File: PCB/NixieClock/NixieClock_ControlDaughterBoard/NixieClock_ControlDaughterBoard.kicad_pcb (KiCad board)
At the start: 2 copper layers, 85 x 50 mm, 30 parts, among them J1 Conn_01x05, J3 Conn_01x04_Pin, J4 Conn_01x04_Pin, Q1 IRLML6244, Q2 IRLML6244

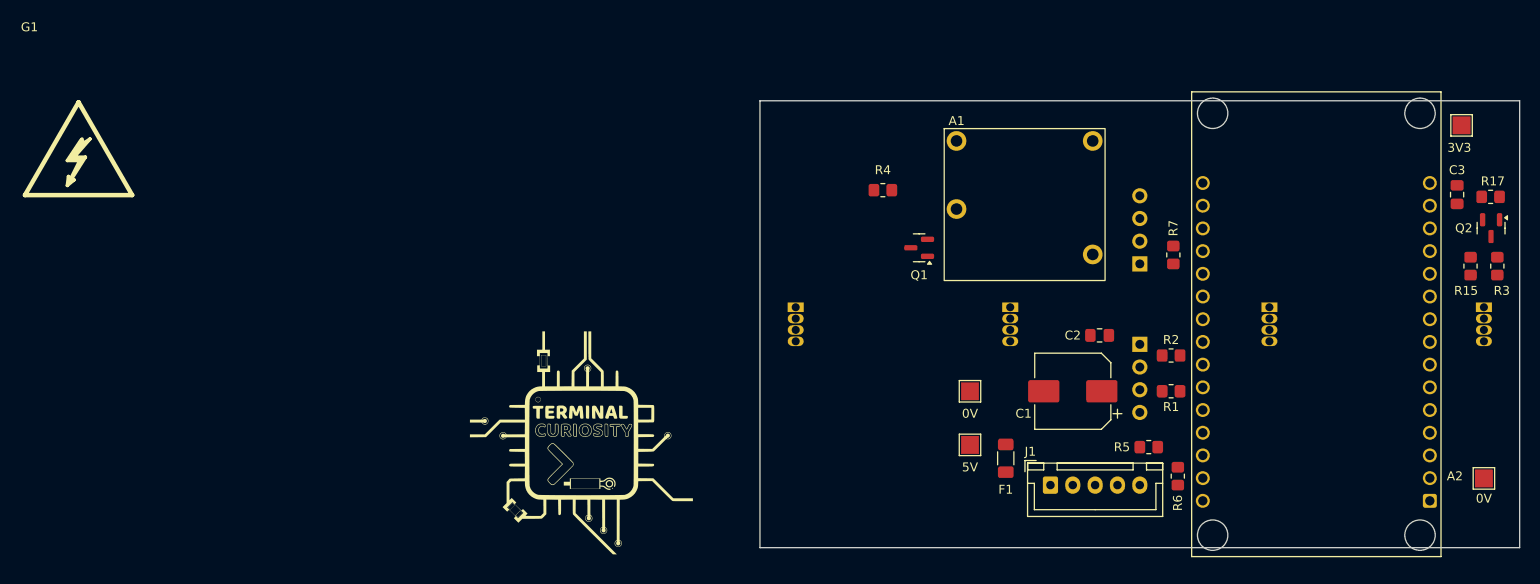
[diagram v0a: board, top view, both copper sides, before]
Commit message: Layout WIP
layout half completed.
+5V net class added to SCH so it has thicker traces on PCB
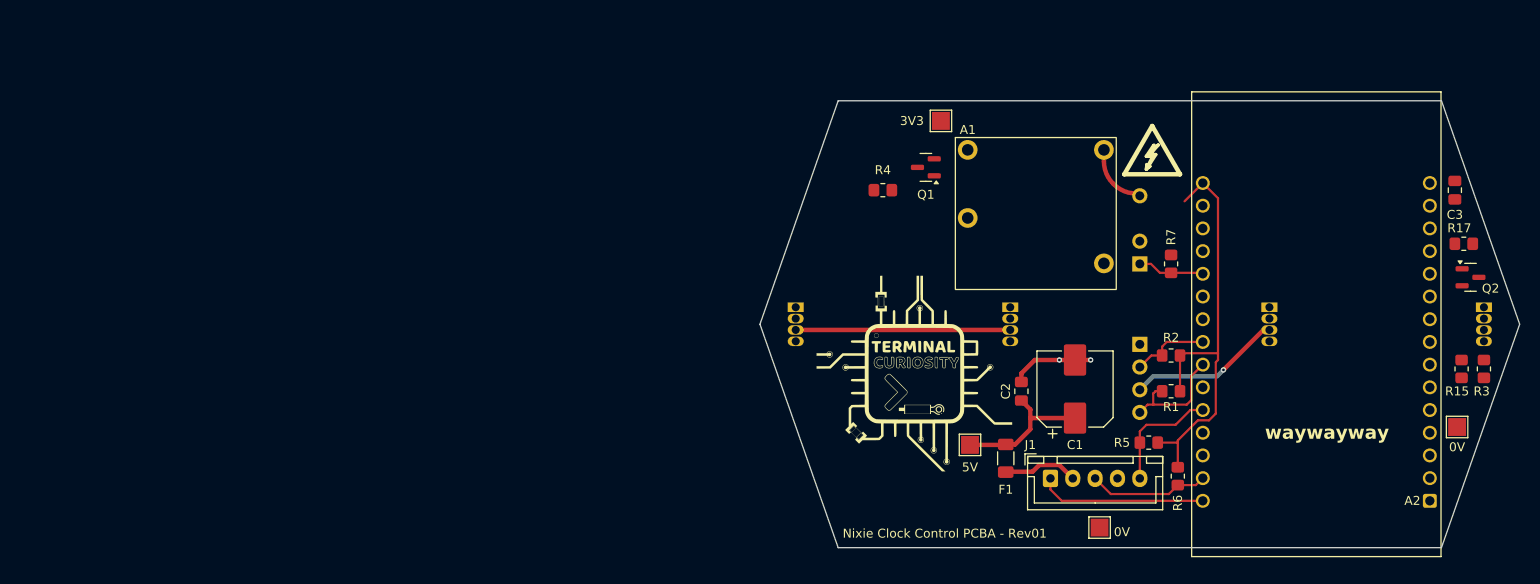
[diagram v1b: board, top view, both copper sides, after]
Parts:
- moved G1 120.2 mm to (144.0, 92.2)
- moved TP2 58.3 mm to (126.2, 82.2)
- moved G2 38.0 mm to (123.2, 110.5)
- moved TP5 21.0 mm to (144.0, 127.8)
- moved R3 11.6 mm to (187.0, 110.0), turned to 90 degrees
- moved R15 11.5 mm to (184.5, 110.0), turned to -90 degrees
- moved C2 10.8 mm to (135.2, 112.5), turned to 90 degrees
- moved Q1 9.03 mm to (124.6, 87.5)
- moved TP6 6.49 mm to (184.0, 116.5)
- moved R17 6.05 mm to (184.8, 96.0), turned to 0 degrees
- moved Q2 5.96 mm to (185.5, 99.8), turned to 0 degrees
- moved A1 1.60 mm to (127.9, 84.1)
- moved R7 1.03 mm to (152.0, 98.2)
- moved J1 0.75 mm to (138.5, 122.2)
- moved C3 0.56 mm to (183.8, 90.0)
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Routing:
- net +5V: track 0.00 -> 57.4 mm, vias 0 -> 1
- net +3.3V: track 0.00 -> 48.9 mm
- net /INT2: track 0.00 -> 18.8 mm
- net /I2C_SCL2: track 0.00 -> 13.5 mm
- net /I2C_SDA2: track 0.00 -> 13.3 mm
- net /I2C_SCL1: track 0.00 -> 13.2 mm
- net GND: track 0.00 -> 9.33 mm, vias 0 -> 2
- net /I2C_SDA1: track 0.00 -> 8.80 mm
- net /5V_IN: track 0.00 -> 8.43 mm
- net /LDR_IN: track 0.00 -> 7.51 mm
- net Net-(A1-VOUT): track 0.00 -> 6.19 mm
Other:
- outline, holes or cut-outs redrawn
- board text added: "Nixie Clock Control PCBA - Rev01"
- board text added: "waywayway"

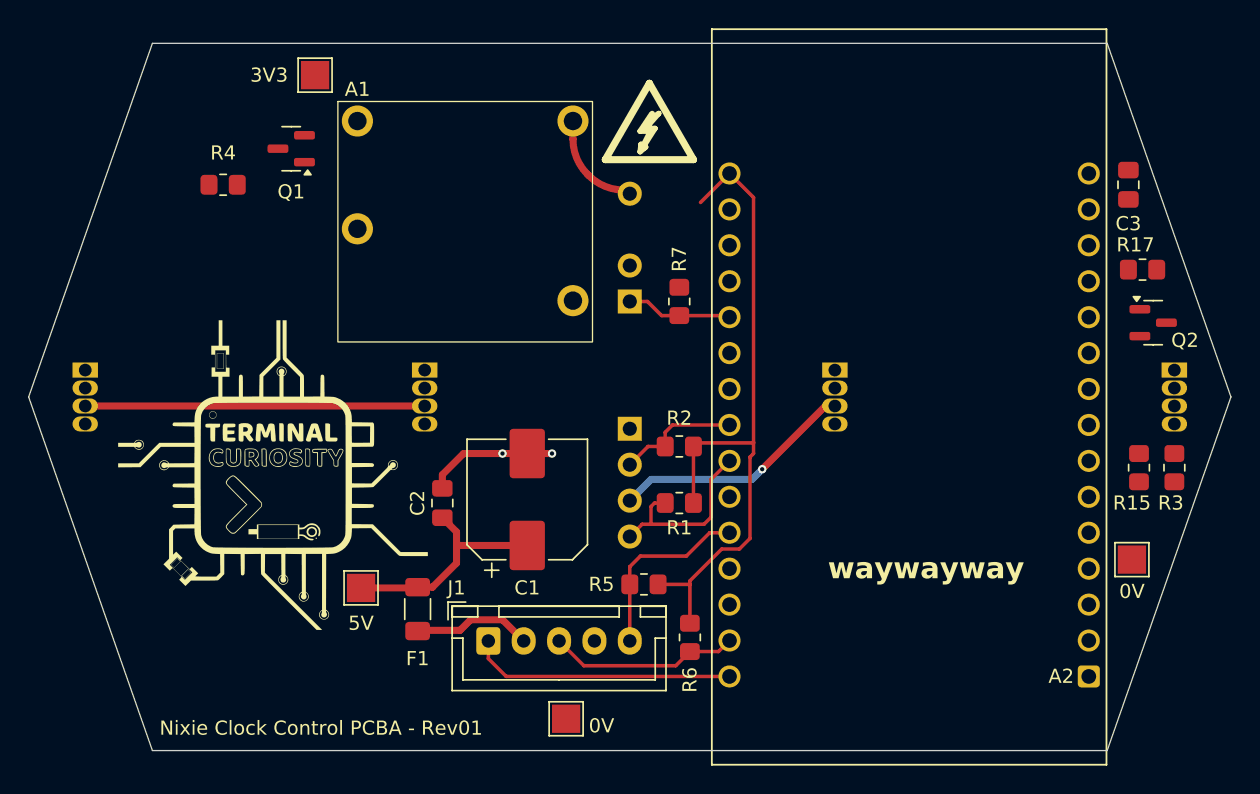
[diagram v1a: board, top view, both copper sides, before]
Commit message: layout draft1 complete
completed all pcb routing and polygon pour.
Changed LED footprints to wide pins. previously they had 0.085mm clearance between pads, which is too tight to manufacture. wide pins have 0.36mm min (14mil) which is above PCBway suggested 6mil.
Removed all DRC errors.
Some warnings exist for ESP32 silkscreen beyond board border, but this is ok for the assembly overall
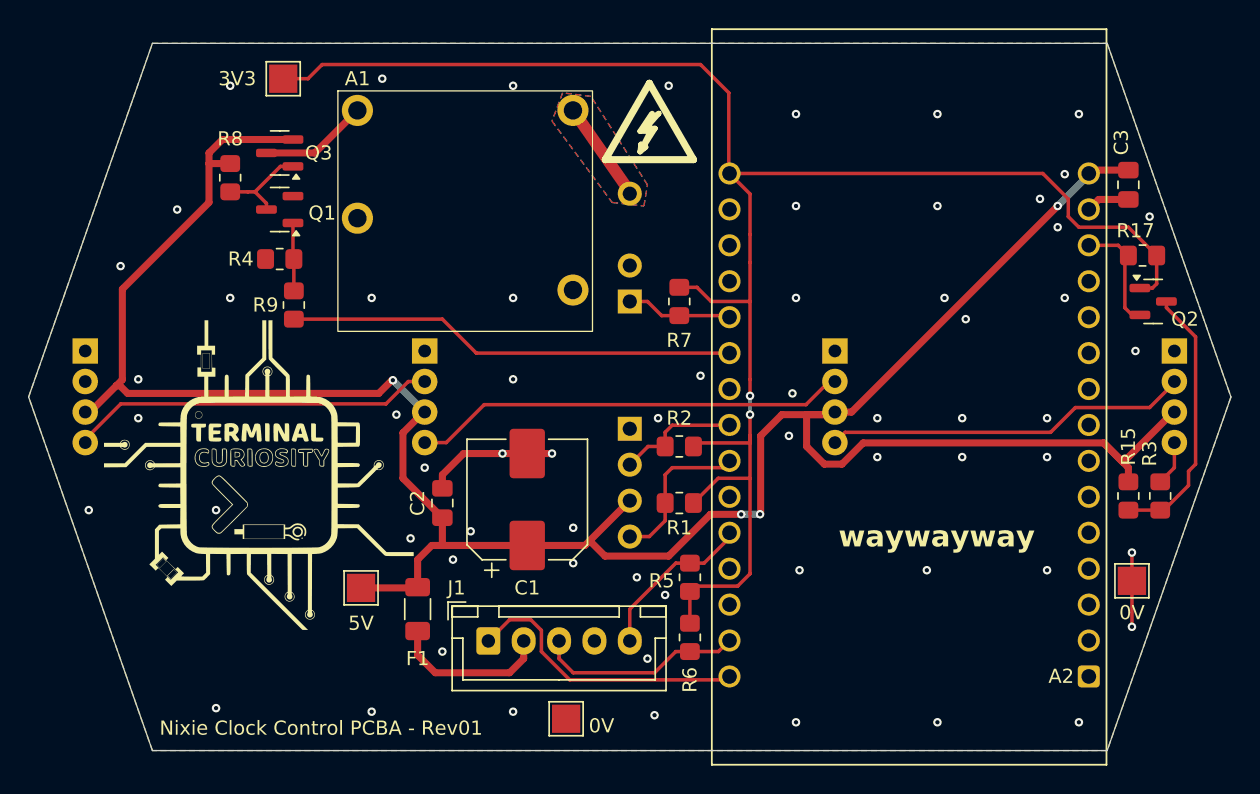
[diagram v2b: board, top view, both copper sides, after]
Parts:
- added Q3: IRLML6402, Package_TO_SOT_SMD:SOT-23, F.Cu at (123.8, 87.8)
- added R8: 10k, Resistor_SMD:R_0805_2012Metric_Pad1.20x1.40mm_HandSolder, F.Cu at (120.2, 89.5)
- added R9: 470R, Resistor_SMD:R_0805_2012Metric_Pad1.20x1.40mm_HandSolder, F.Cu at (124.8, 98.5)
- D1, D2, D3, D4: footprint LED_THT:LED_D5.0mm-4_RGB -> LED_THT:LED_D5.0mm-4_RGB_Wide_Pins
- moved R4 6.60 mm to (123.8, 95.2), turned to 180 degrees
- moved Q1 4.38 mm to (123.8, 91.8)
- moved R5 3.29 mm to (152.8, 117.8), turned to 90 degrees
- moved TP2 2.26 mm to (124.0, 82.5)
- moved R3 2.24 mm to (186.0, 112.0)
- moved R15 2.14 mm to (183.8, 112.0)
- moved Q2 1.50 mm to (185.5, 98.2)
- moved TP6 1.50 mm to (184.0, 118.0)
- moved D1 1.35 mm to (187.0, 101.8)
- moved D2 1.35 mm to (163.0, 101.8)
- moved D3 1.35 mm to (134.0, 101.8)
- moved D4 1.35 mm to (110.0, 101.8)
- moved G2 1.00 mm to (122.2, 110.5)
- moved R17 1.00 mm to (184.8, 95.0), turned to 180 degrees
- moved A1 0.75 mm to (127.9, 83.4)
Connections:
- A1 pad 1: +5V -> Net-(A1-VIN)
- A1 pad 2: Net-(Q1-D) -> GND
- Q1 pad 1: Net-(A2-GPIO16/RX2) -> Net-(Q1-G)
- R4 pad 1: Net-(A2-GPIO16/RX2) -> Net-(Q1-G)
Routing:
- net +5V: track 57.4 -> 177.8 mm, vias 1 -> 4
- net +3.3V: track 48.9 -> 125.8 mm, vias 0 -> 2
- net Net-(A2-GPIO16/RX2): track 0.00 -> 32.1 mm
- net Net-(D2-DOUT): track 0.77 -> 31.0 mm
- net Net-(D3-DOUT): track 0.00 -> 26.1 mm
- net Net-(D1-DOUT): track 0.00 -> 25.6 mm
- net /LED-Data_5V: track 0.00 -> 19.0 mm
- net GND: track 9.33 -> 17.7 mm, vias 2 -> 63
- net /LED-Data_3V3: track 0.00 -> 8.17 mm
- net Net-(A1-VIN): track 0.00 -> 7.68 mm
- net Net-(Q1-D): track 0.00 -> 6.77 mm
- net Net-(Q1-G): track 0.00 -> 4.83 mm
- net Net-(D1-DIN): track 0.00 -> 3.19 mm
- net /5V_IN: track 8.43 -> 11.4 mm
- net /I2C_SCL1: track 13.2 -> 11.2 mm
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- added copper zone on B.Cu, net GND
- added copper zone on F.Cu, net GND
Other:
- board text added: "OK to add teardrops"

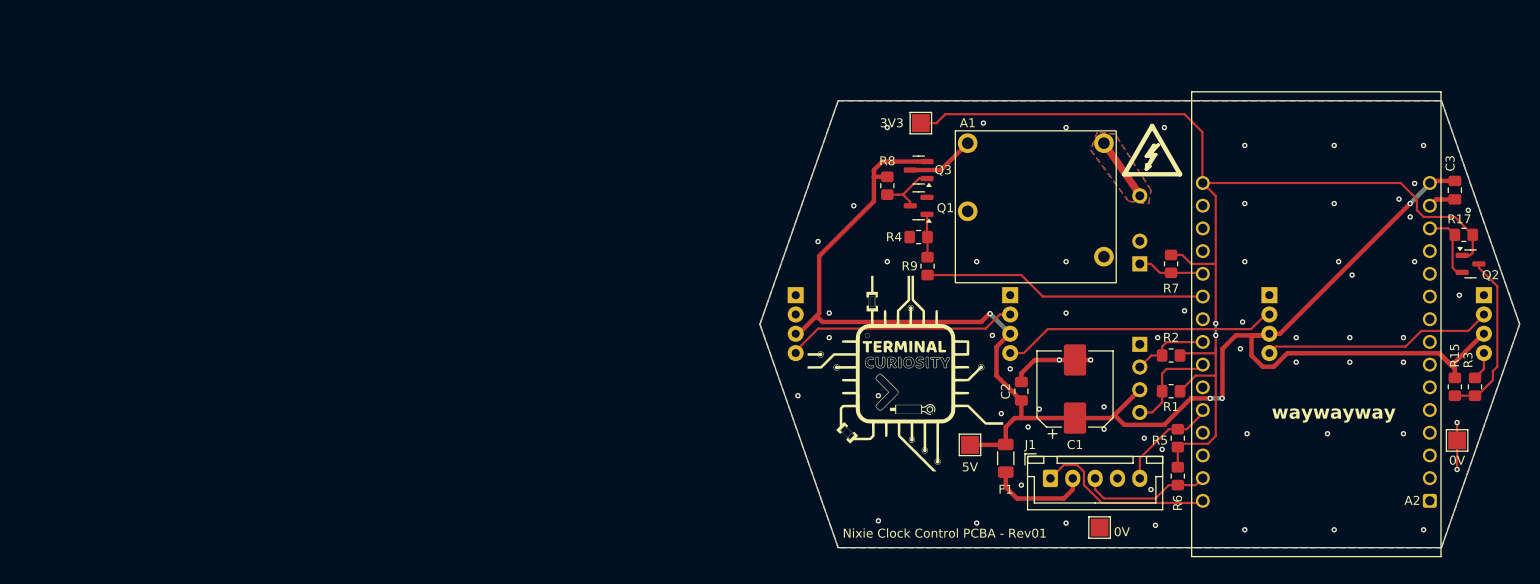
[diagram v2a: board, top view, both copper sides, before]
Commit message: PCB layout 2 complete
layout 1 was incorrect as the connectors and LEDs were not located in the right place to correctly mate with the tube panel PCBA. When connectors and LEDs were moved, all the traces became scrambled. it was necessary to re-wire the entire board.
ESP32 pins were also remapped to improve ease of wiring
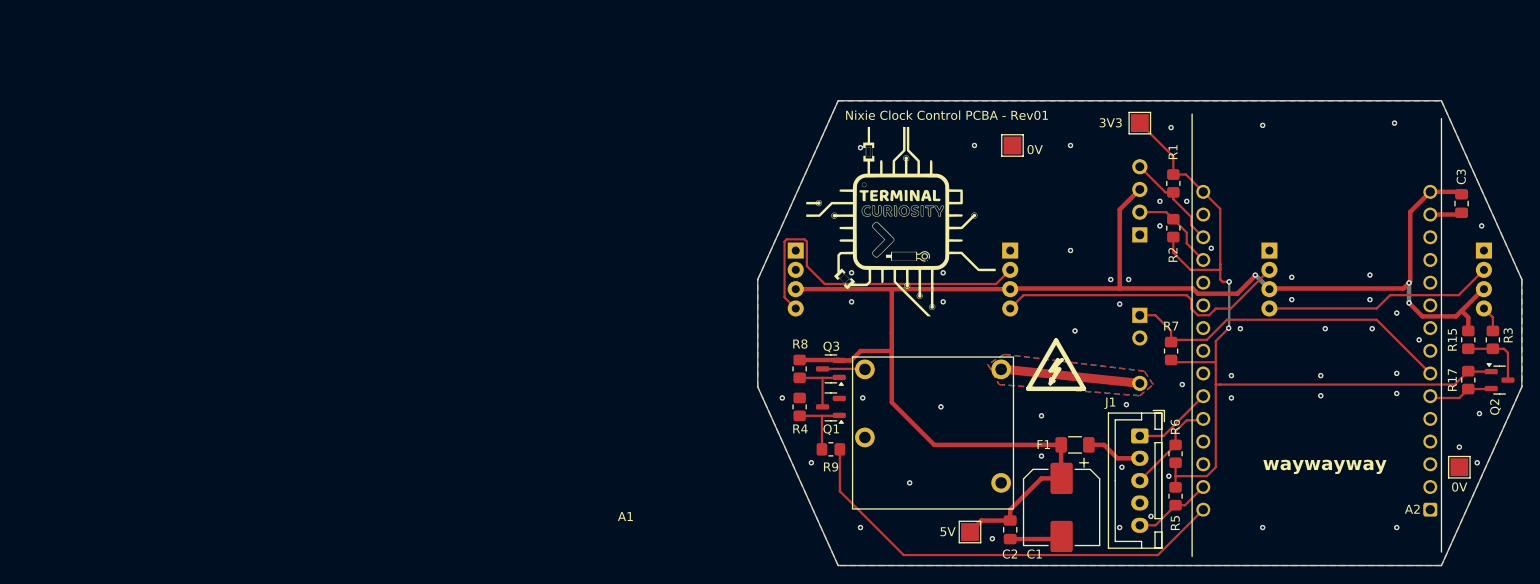
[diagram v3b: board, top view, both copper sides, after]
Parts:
- moved TP5 43.8 mm to (134.2, 85.0)
- moved A1 27.8 mm to (116.4, 108.7)
- moved G1 26.3 mm to (133.2, 116.2)
- moved Q1 24.5 mm to (113.9, 114.2)
- moved TP2 24.5 mm to (148.5, 82.5)
- moved Q3 24.3 mm to (113.9, 110.0)
- moved R1 23.3 mm to (152.2, 89.2), turned to -90 degrees
- moved R4 23.2 mm to (110.4, 114.2), turned to 90 degrees
- moved R9 23.2 mm to (113.9, 119.0), turned to 180 degrees
- moved R8 22.7 mm to (110.4, 110.0)
- moved G2 17.0 mm to (121.8, 93.5)
- moved R17 16.3 mm to (185.2, 111.2), turned to -90 degrees
- moved C2 15.6 mm to (134.0, 128.0), turned to -90 degrees
- moved R2 14.3 mm to (152.2, 94.2), turned to 90 degrees
- moved Q2 13.4 mm to (188.8, 111.2)
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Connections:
- A2 pad 13: /LED-Data_3V3 -> unconnected-(A2-GPIO13-Pad13)
- A2 pad 18: unconnected-(A2-GPIO15-Pad18) -> /I2C_SCL1
- A2 pad 19: unconnected-(A2-GPIO2-Pad19) -> /I2C_SDA1
- A2 pad 20: /LDR_IN -> unconnected-(A2-GPIO4-Pad20)
- A2 pad 21: Net-(A2-GPIO16/RX2) -> unconnected-(A2-GPIO16/RX2-Pad21)
- A2 pad 23: /I2C_SDA1 -> unconnected-(A2-GPIO5-Pad23)
- A2 pad 24: /I2C_SCL1 -> unconnected-(A2-GPIO18-Pad24)
- A2 pad 25: unconnected-(A2-GPIO19-Pad25) -> /INT2
- A2 pad 30: /INT2 -> Net-(A2-GPIO23)
- A2 pad 6: unconnected-(A2-GPIO32-Pad6) -> /LED-Data_3V3
- A2 pad 7: unconnected-(A2-GPIO33-Pad7) -> /LDR_IN
- J1 pad 3: /I2C_SCL2 -> /I2C_SDA2
- J1 pad 5: /I2C_SDA2 -> /I2C_SCL2
- R5 pad 2: /I2C_SDA2 -> /I2C_SCL2
- R6 pad 2: /I2C_SCL2 -> /I2C_SDA2
- R9 pad 1: Net-(A2-GPIO16/RX2) -> Net-(A2-GPIO23)
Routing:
- net Net-(A2-GPIO23): track 0.00 -> 50.4 mm
- net Net-(A2-GPIO16/RX2): track 32.1 -> 0.00 mm
- net /LDR_IN: track 7.51 -> 37.6 mm
- net +3.3V: track 125.8 -> 97.1 mm
- net Net-(D3-DOUT): track 26.1 -> 37.7 mm
- net /INT2: track 20.4 -> 8.94 mm
- net /LED-Data_5V: track 19.0 -> 7.68 mm
- net Net-(A1-VOUT): track 7.05 -> 15.7 mm
- net GND: track 17.7 -> 9.45 mm, vias 63 -> 55
- net /I2C_SCL2: track 14.7 -> 8.88 mm
- net /5V_IN: track 11.4 -> 6.32 mm
- net +5V: track 177.8 -> 174.3 mm, vias 4 -> 3
- net Net-(Q1-G): track 4.83 -> 7.91 mm
- net Net-(A1-VIN): track 7.68 -> 4.76 mm
- net Net-(D2-DOUT): track 31.0 -> 33.2 mm
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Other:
- board size 85 x 50 mm -> 85.5 x 52 mm

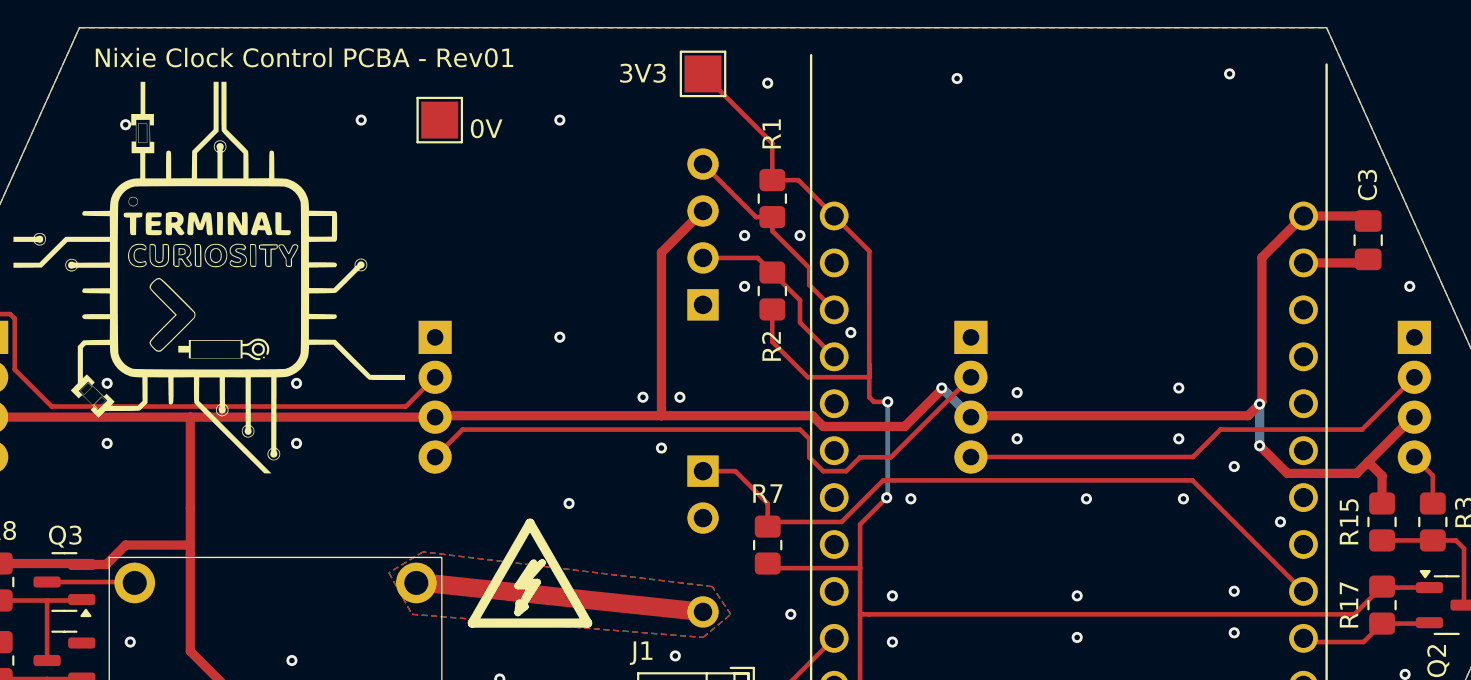
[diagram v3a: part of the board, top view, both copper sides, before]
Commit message: I2C pin remap based on breadboard tests
tested I2C pin mappings on breadboard and found that using GPIO2 caused the board to get stuck in boot mode. remapped to adjacent pin GPIO4 for safety.
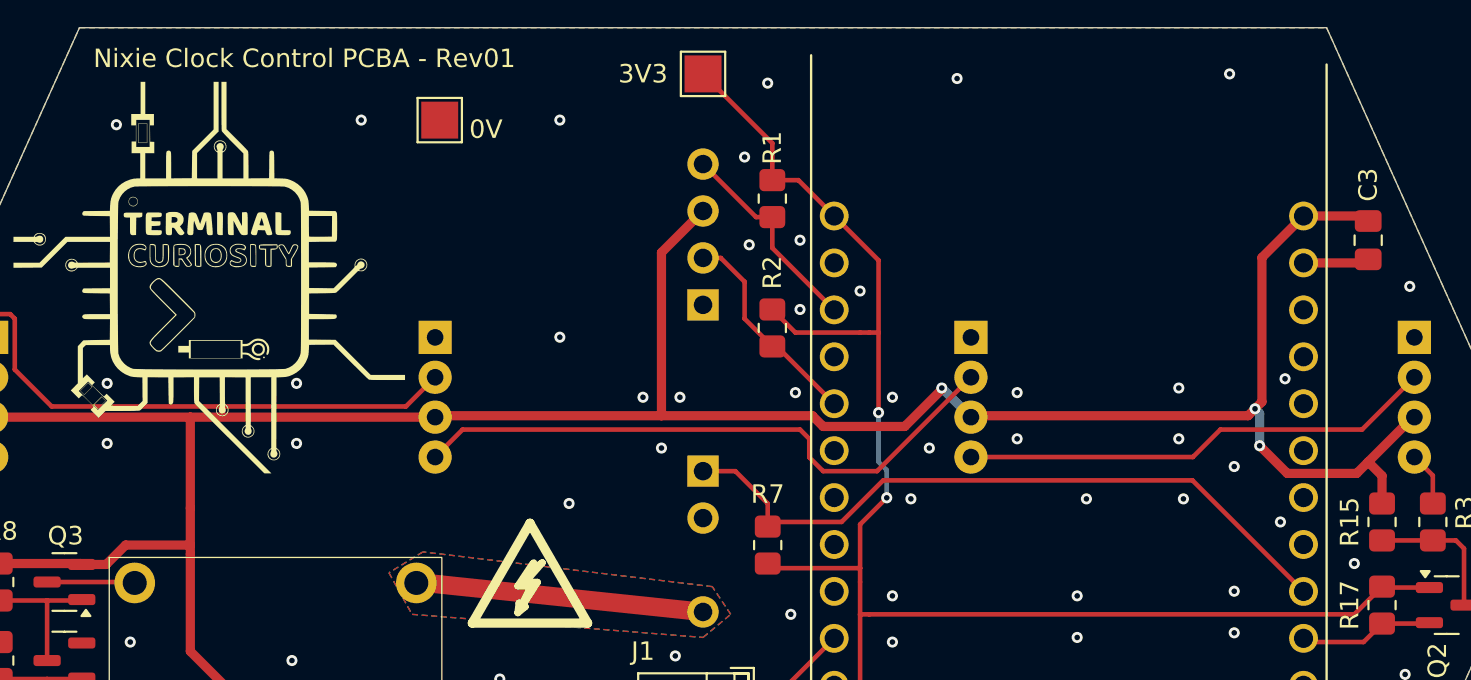
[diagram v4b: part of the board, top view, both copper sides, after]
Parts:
- moved R2 2.00 mm to (152.2, 96.2), turned to -90 degrees
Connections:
- A2 pad 19: /I2C_SDA1 -> unconnected-(A2-GPIO2-Pad19)
- A2 pad 20: unconnected-(A2-GPIO4-Pad20) -> /I2C_SDA1
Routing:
- net +3.3V: track 97.1 -> 94.4 mm
- net /I2C_SDA1: track 10.0 -> 11.5 mm
- net GND: vias 55 -> 61
